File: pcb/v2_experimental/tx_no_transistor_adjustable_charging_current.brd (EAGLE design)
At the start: 28 x 36.5 mm, 56 parts, among them IC1 STM32F030F4, IC2 NRF24L01ALT1, SW2 324_SW324_SWITCH_FOOT_HOLE, U2 USBC_16P, U3 MCP73831T-2ACI/OT, U4 XC6206_DEV, Y1 16MHz_12pF

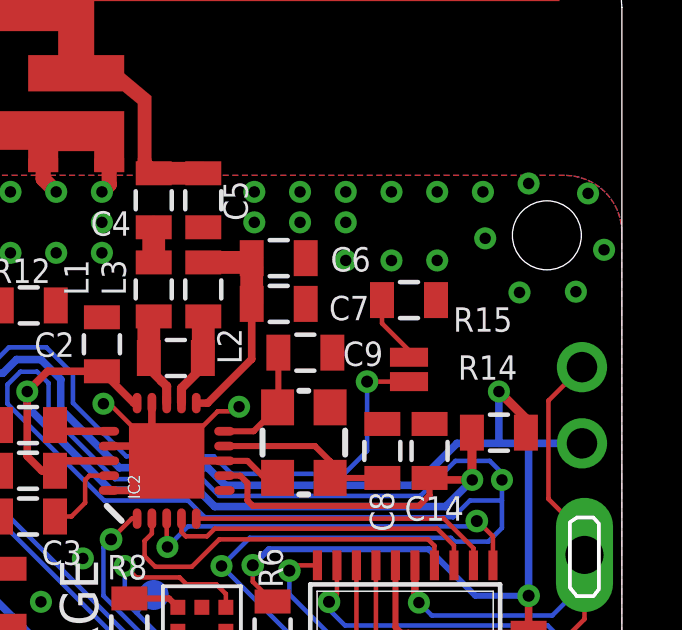
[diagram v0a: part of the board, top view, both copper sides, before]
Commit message: added adjustable charging current select
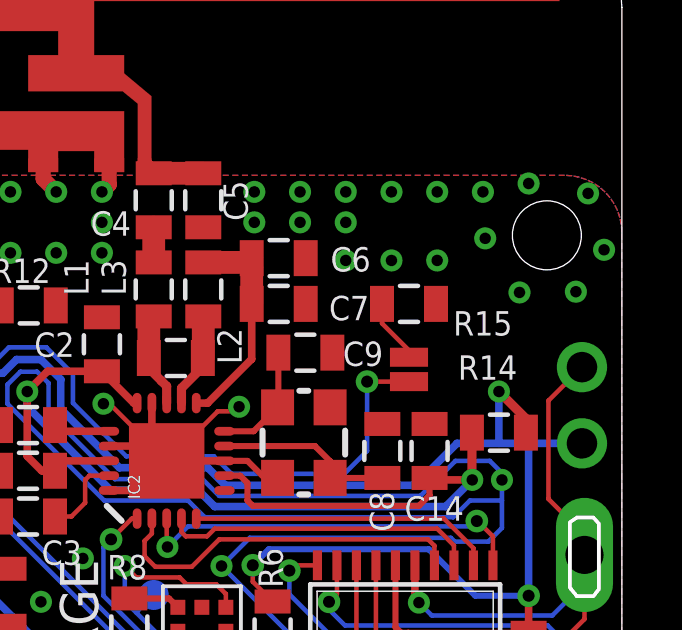
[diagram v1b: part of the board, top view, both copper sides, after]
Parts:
- moved R15 0.13 mm to (20.9, 24.7)
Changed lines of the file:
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@@
 </element>
 <element name="JP2" library="SparkFun-Jumpers" package="SMT-JUMPER_2_NO_NO-SILK" value="JUMPER-SMT_2_NO_NO-SILK" x="20.9042" y="22.5298" smashed="yes" rot="R270"/>
-<element name="R15" library="SparkFun-Passives" package="0805" value="22K" x="20.9042" y="24.8412" smashed="yes">
-<attribute name="NAME" x="22.3774" y="23.7871" size="0.8128" layer="25"/>
+<element name="R15" library="SparkFun-Passives" package="0805" value="22K" x="20.9042" y="24.7142" smashed="yes">
+<attribute name="NAME" x="22.3774" y="23.6601" size="0.8128" layer="25"/>
 </element>
 </elements>
@@
 <wire x1="20.9042" y1="22.9362" x2="20.9042" y2="23.1648" width="0.1524" layer="1"/>
 <wire x1="20.9042" y1="23.1648" x2="20.0042" y2="24.0648" width="0.1524" layer="1"/>
-<wire x1="20.0042" y1="24.0648" x2="20.0042" y2="24.8412" width="0.1524" layer="1"/>
+<wire x1="20.0042" y1="24.0648" x2="20.0042" y2="24.7142" width="0.1524" layer="1"/>
 </signal>
 </signals>
